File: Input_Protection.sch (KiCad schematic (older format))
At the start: 125 parts, among them U201 MOCD217M, U202 MOCD217M, U203 MOCD217M, U204 MOCD217M, U205 MOCD217M, U206 MOCD217M, U207 MOCD217M, U208 MOCD217M, U209 MOCD217M, U210 MOCD217M, U211 MOCD217M, U212 MOCD217M, U213 MOCD217M, U214 MOCD217M, U215 MOCD217M, U216 MOCD217M, U217 MOCD217M, U218 MOCD217M, U219 MOCD217M, U220 MOCD217M, U221 MOCD217M, U222 MOCD217M, U223 MOCD217M, U224 MOCD217M, U225 MOCD217M

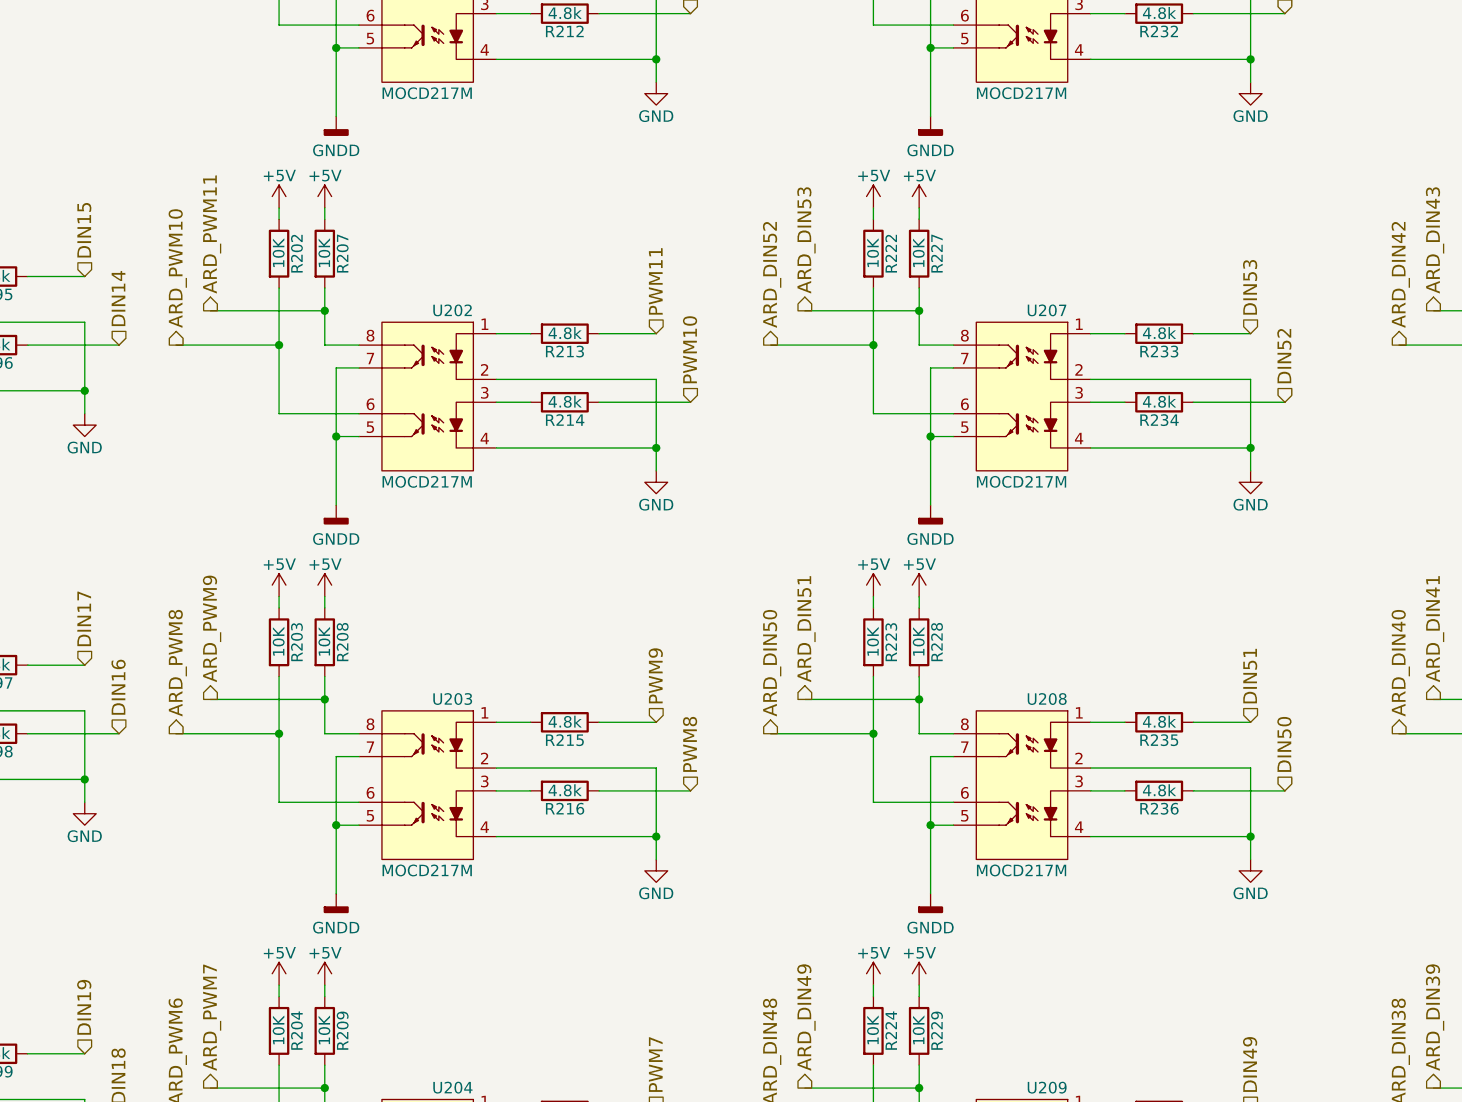
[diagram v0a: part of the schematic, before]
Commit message: connecting spi lines and cleaning-up I/O
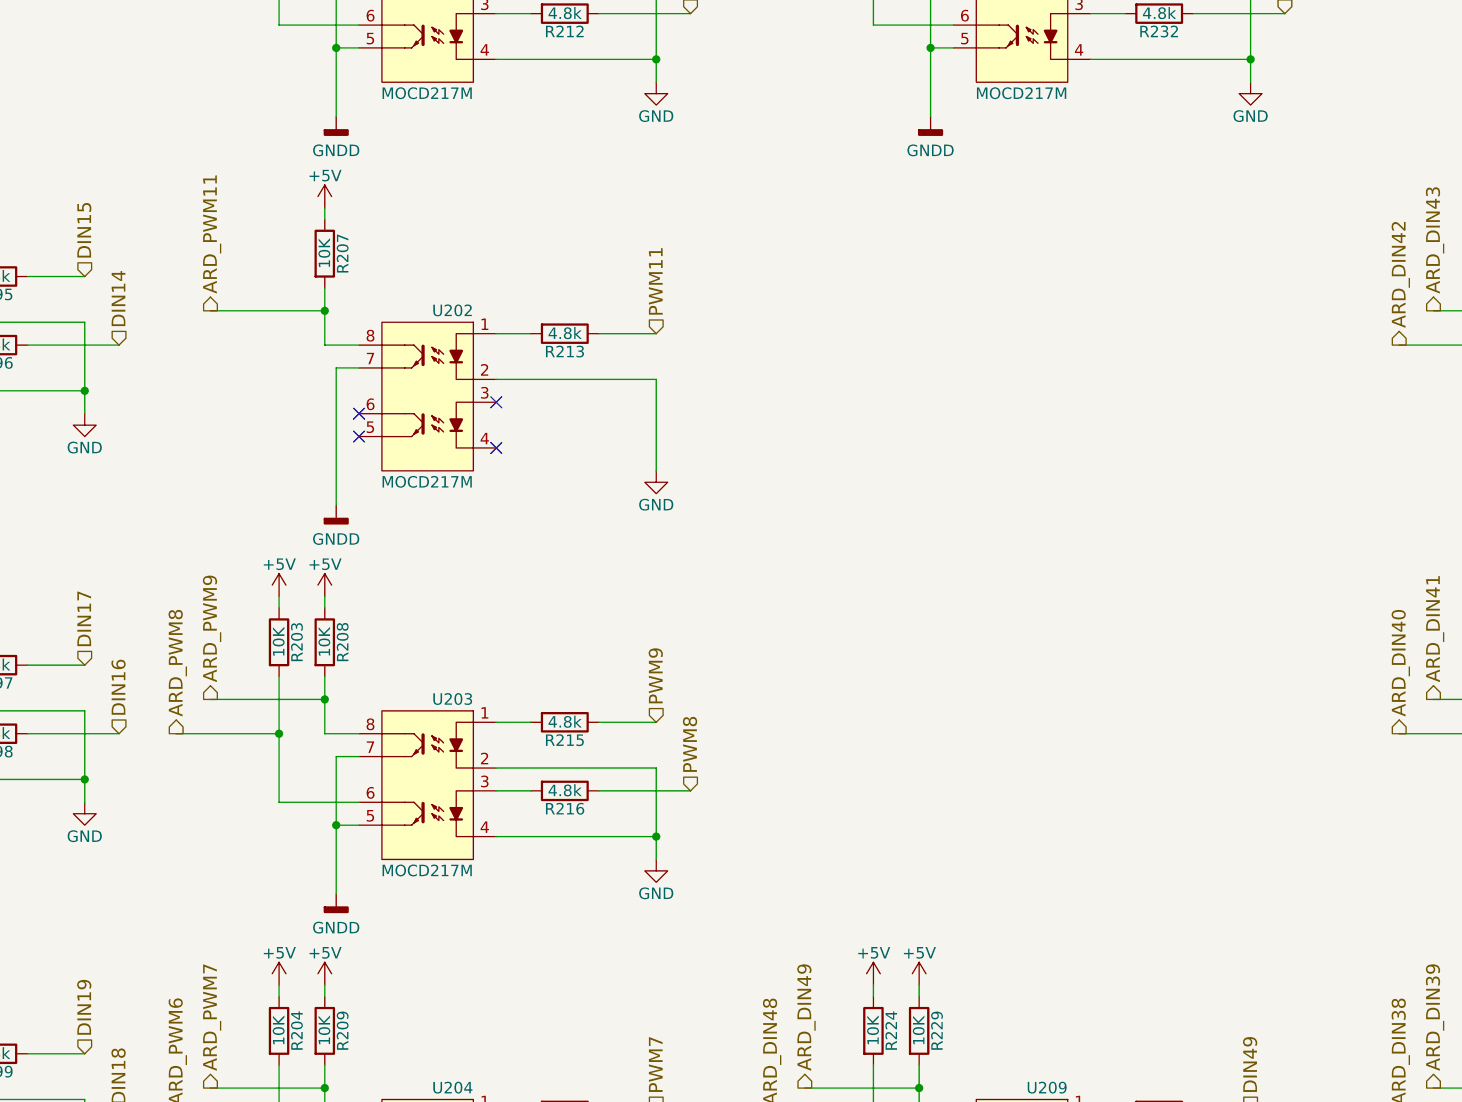
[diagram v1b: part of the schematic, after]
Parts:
- removed R202, R222, R223, R227, R228: 10K, Resistors_SMD:R_0805, symbol R
- removed R214, R233, R234, R235, R236: 4.8k, Resistors_SMD:R_1206, symbol R
- removed U207, U208: MOCD217M, Housings_SOIC:SOIC-8_3.9x4.9mm_Pitch1.27mm, symbol MOCD213M
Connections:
- net GND: no longer U202.4
- net GNDD: no longer U202.5
- net ARD_PWM10: no longer names the net of U202.6
- no-connect marks 0 -> 4

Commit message: adding global hardware library, also fixed some footprint issues and added reverse protection diodes. also cleaned-up design
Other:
- moved on the sheet: R201, R203, R204, R205, R206, R207, R208, R209, R210, R211, R212, R213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
